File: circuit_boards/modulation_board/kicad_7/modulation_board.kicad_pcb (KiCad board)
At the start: 2 copper layers, 0 parts

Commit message: Progress on circuit boards
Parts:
- added C1001: 10u, Capacitor_THT:CP_Radial_D6.3mm_P2.50mm, B.Cu at (116.4, 143.8)
- added C1002: 10u, Capacitor_THT:CP_Radial_D6.3mm_P2.50mm, B.Cu at (95.3, 143.8)
- added C1003: 470n, Capacitor_SMD:C_0805_2012Metric, B.Cu at (86.1, 125.1)
- added C1004: 470n, Capacitor_SMD:C_0805_2012Metric, B.Cu at (89.9, 136.2)
- added C1005: 100n, Capacitor_SMD:C_0603_1608Metric, B.Cu at (90.9, 125.1)
- added C1006: 100n, Capacitor_SMD:C_0603_1608Metric, B.Cu at (84.9, 136.0)
- added C1007: 2u2, Capacitor_SMD:C_0805_2012Metric, B.Cu at (87.1, 106.3)
- added C1008: 100n, Capacitor_SMD:C_0603_1608Metric, B.Cu at (91.9, 106.3)
- added C1009: 100n, Capacitor_SMD:C_0603_1608Metric, B.Cu at (60.9, 109.2)
- added C1010: 100n, Capacitor_SMD:C_0603_1608Metric, B.Cu at (66.0, 109.2)
- added C1011: 100n, Capacitor_SMD:C_0603_1608Metric, B.Cu at (77.7, 141.0)
- added C1012: 100n, Capacitor_SMD:C_0603_1608Metric, B.Cu at (82.5, 141.0)
- added C1013: 100n, Capacitor_SMD:C_0603_1608Metric, B.Cu at (97.3, 51.4)
- added C1014: 100n, Capacitor_SMD:C_0603_1608Metric, B.Cu at (102.4, 51.4)
- added C1015: 100n, Capacitor_SMD:C_0603_1608Metric, B.Cu at (110.7, 79.7)
- added C1016: 100n, Capacitor_SMD:C_0603_1608Metric, B.Cu at (89.5, 73.8)
- added C1017: 100n, Capacitor_SMD:C_0603_1608Metric, B.Cu at (73.8, 164.9)
- added C1018: 100n, Capacitor_SMD:C_0603_1608Metric, B.Cu at (78.5, 176.8)
- added C301: 100n, Capacitor_SMD:C_0603_1608Metric, B.Cu at (121.4, 116.3)
- added C302: 4p3, Capacitor_SMD:C_0603_1608Metric, B.Cu at (125.2, 110.5)
- added C303: 4p3, Capacitor_SMD:C_0603_1608Metric, B.Cu at (125.2, 113.3)
- added C304: 100n, Capacitor_SMD:C_0603_1608Metric, B.Cu at (133.1, 78.2)
- added C305: 100n, Capacitor_SMD:C_0603_1608Metric, B.Cu at (148.8, 51.6)
- added C306: 100n, Capacitor_SMD:C_0603_1608Metric, B.Cu at (110.2, 115.8)
- added C307: 1u, Capacitor_SMD:C_0805_2012Metric, B.Cu at (106.9, 115.8)
- added C308: 10u, Capacitor_SMD:C_0805_2012Metric, B.Cu at (105.2, 112.3)
- added C309: 100n, Capacitor_SMD:C_0603_1608Metric, B.Cu at (121.4, 119.1)
- added C310: 10u, Capacitor_SMD:C_0805_2012Metric, B.Cu at (121.4, 122.2)
- added C401: 100n, Capacitor_SMD:C_0603_1608Metric, B.Cu at (57.7, 66.0)
- added C402: 100n, Capacitor_SMD:C_0603_1608Metric, B.Cu at (79.5, 65.8)
- added C403: 100n, Capacitor_SMD:C_0603_1608Metric, B.Cu at (101.6, 65.8)
- added C404: 100n, Capacitor_SMD:C_0603_1608Metric, B.Cu at (124.0, 65.5)
- added C405: 100n, Capacitor_SMD:C_0603_1608Metric, B.Cu at (57.1, 95.5)
- added C406: 100n, Capacitor_SMD:C_0603_1608Metric, B.Cu at (79.5, 94.7)
- added C407: 100n, Capacitor_SMD:C_0603_1608Metric, B.Cu at (101.6, 95.5)
- added C408: 100n, Capacitor_SMD:C_0603_1608Metric, B.Cu at (124.0, 96.0)
- added C409: 100n, Capacitor_SMD:C_0603_1608Metric, B.Cu at (109.2, 139.2)
- added C410: 100n, Capacitor_SMD:C_0603_1608Metric, B.Cu at (125.2, 138.7)
- added C411: 100n, Capacitor_SMD:C_0603_1608Metric, B.Cu at (142.7, 158.8)
- added C412: 100n, Capacitor_SMD:C_0603_1608Metric, B.Cu at (57.7, 36.8)
- added C413: 100n, Capacitor_SMD:C_0603_1608Metric, B.Cu at (84.8, 80.4)
- added C414: 100n, Capacitor_SMD:C_0603_1608Metric, B.Cu at (93.0, 77.6)
- added C501: 100n, Capacitor_SMD:C_0603_1608Metric, B.Cu at (111.0, 119.9)
- added C601: 10u, Capacitor_SMD:C_0805_2012Metric, B.Cu at (124.7, 91.4)
- added C602: 1u, Capacitor_SMD:C_0805_2012Metric, B.Cu at (109.0, 97.5)
- added C603: 10u, Capacitor_SMD:C_0805_2012Metric, B.Cu at (54.6, 84.6)
- added C604: 10u, Capacitor_SMD:C_0805_2012Metric, B.Cu at (54.6, 78.5)
- added C605: 1n, Capacitor_SMD:C_0603_1608Metric, B.Cu at (72.1, 110.5)
- added C606: 1n, Capacitor_SMD:C_0603_1608Metric, B.Cu at (54.7, 112.8)
- added C607: 1n, Capacitor_SMD:C_0603_1608Metric, B.Cu at (72.1, 102.1)
- added C608: 1n, Capacitor_SMD:C_0603_1608Metric, B.Cu at (54.7, 101.6)
- added C609: 100n, Capacitor_SMD:C_0603_1608Metric, B.Cu at (115.6, 87.5)
- added C610: 1u, Capacitor_SMD:C_0805_2012Metric, B.Cu at (115.6, 84.4)
- added C611: 100n, Capacitor_SMD:C_0603_1608Metric, B.Cu at (53.8, 119.9)
- added C612: 100n, Capacitor_SMD:C_0603_1608Metric, B.Cu at (109.0, 103.9)
- added C613: 100n, Capacitor_SMD:C_0603_1608Metric, B.Cu at (54.6, 74.4)
- added C614: 1u, Capacitor_SMD:C_0805_2012Metric, B.Cu at (109.0, 100.8)
- added C615: 100n, Capacitor_SMD:C_0603_1608Metric, B.Cu at (55.4, 137.9)
- added C616: 100n, Capacitor_SMD:C_0603_1608Metric, B.Cu at (54.1, 132.8)
- added C617: 100n, Capacitor_SMD:C_0603_1608Metric, B.Cu at (111.6, 174.0)
- added C618: 100n, Capacitor_SMD:C_0603_1608Metric, B.Cu at (146.8, 130.8)
- added C701: 100n, Capacitor_SMD:C_0603_1608Metric, B.Cu at (144.0, 104.7)
- added C801: 10n, Capacitor_SMD:C_0603_1608Metric, B.Cu at (77.7, 159.8)
- added C802: 47n COG, Capacitor_SMD:C_0805_2012Metric, B.Cu at (72.4, 176.5)
- added C803: 100p, Capacitor_SMD:C_0603_1608Metric, B.Cu at (87.9, 140.7)
- added C804: 100p, Capacitor_SMD:C_0603_1608Metric, B.Cu at (72.9, 143.5)
- added C805: 10u, Capacitor_SMD:C_0805_2012Metric, B.Cu at (48.1, 183.2)
- added C901: 100p, Capacitor_SMD:C_0603_1608Metric, B.Cu at (107.3, 43.4)
- added C902: 100p, Capacitor_SMD:C_0603_1608Metric, B.Cu at (93.0, 43.4)
- added C903: 100p, Capacitor_SMD:C_0603_1608Metric, B.Cu at (96.3, 65.9)
- added D301: 1N4148W, Diode_SMD:D_SOD-123, B.Cu at (141.2, 75.2)
- added D701: LED, LED_THT:LED_D3.0mm, F.Cu at (147.9, 40.0)
- added D702: LED, LED_THT:LED_D3.0mm, F.Cu at (147.9, 71.8)
- added D703: LED, LED_THT:LED_D3.0mm, F.Cu at (147.9, 100.3)
- added D704: LED, LED_THT:LED_D3.0mm, F.Cu at (85.1, 111.8)
- added D705: LED, LED_THT:LED_D3.0mm, F.Cu at (98.4, 134.0)
- added FB1001: 100R @ 100MHz, Inductor_SMD:L_0805_2012Metric, B.Cu at (90.9, 110.7)
- added FB1002: 100R @ 100MHz, Inductor_SMD:L_0805_2012Metric, B.Cu at (116.6, 120.7)
- added FB301: 1k@100MHz, Inductor_SMD:L_0805_2012Metric, B.Cu at (134.1, 66.0)
- added FB302: 1k@100MHz, Inductor_SMD:L_0805_2012Metric, B.Cu at (134.1, 63.0)
- added FB303: 1k@100MHz, Inductor_SMD:L_0805_2012Metric, B.Cu at (144.0, 43.2)
- added FB304: 1k@100MHz, Inductor_SMD:L_0805_2012Metric, B.Cu at (144.0, 51.3)
- added J1: MOD_BOARD_EXT_CON, custom_footprints:16_pin_IDC_header, B.Cu at (116.8, 45.1)
- added J2: VCO_BOARD_CON, custom_footprints:40_pin_IDC_header, B.Cu at (48.3, 48.9)
- added J3: VCF_BOARD_CON, custom_footprints:30_pin_IDC-Header, B.Cu at (64.1, 117.5)
- added J301: SWD_header, Connector_PinHeader_2.54mm:PinHeader_1x04_P2.54mm_Vertical, B.Cu at (107.7, 107.7)
- added J4: power_entry, custom_footprints:10_pin_IDC-Header, B.Cu at (101.6, 151.1)
- added Q801: MMBT3904, Package_TO_SOT_SMD:SOT-23, B.Cu at (57.8, 178.1)
- added R301: 220, Resistor_SMD:R_0603_1608Metric, B.Cu at (140.7, 71.6)
- added R302: 10k, Resistor_SMD:R_0603_1608Metric, B.Cu at (118.9, 107.4)
- added R303: 10k, Resistor_SMD:R_0603_1608Metric, B.Cu at (126.5, 73.2)
- added R304: 220, Resistor_SMD:R_0603_1608Metric, B.Cu at (95.8, 103.1)
- added R305: 22, Resistor_SMD:R_0603_1608Metric, B.Cu at (144.0, 46.0)
- added R306: 10, Resistor_SMD:R_0603_1608Metric, B.Cu at (144.0, 48.8)
- added R401: 5k6, Resistor_SMD:R_0603_1608Metric, B.Cu at (84.8, 77.6)
- added R402: 10k, Resistor_SMD:R_0603_1608Metric, B.Cu at (84.8, 83.2)
- added R501: 390, Resistor_SMD:R_0603_1608Metric, B.Cu at (139.9, 166.9)
- added R502: 100k, Resistor_SMD:R_0603_1608Metric, B.Cu at (117.3, 78.6)
- added R503: 100k, Resistor_SMD:R_0603_1608Metric, B.Cu at (103.8, 78.6)
- added R504: 100k, Resistor_SMD:R_0603_1608Metric, B.Cu at (117.3, 75.8)
- added R505: 10k, Resistor_SMD:R_0603_1608Metric, B.Cu at (103.8, 75.8)
- added R506: 1M, Resistor_SMD:R_0603_1608Metric, B.Cu at (117.3, 73.0)
- added R507: 1M, Resistor_SMD:R_0603_1608Metric, B.Cu at (103.8, 73.0)
- added R601: 2k7, Resistor_SMD:R_0603_1608Metric, B.Cu at (128.5, 87.4)
- added R602: 10k, Resistor_SMD:R_0603_1608Metric, B.Cu at (111.2, 87.5)
- added R603: 100k, Resistor_SMD:R_0603_1608Metric, B.Cu at (54.6, 81.5)
- added R604: 100k, Resistor_SMD:R_0603_1608Metric, B.Cu at (54.6, 87.6)
- added R605: 20k, Resistor_SMD:R_0603_1608Metric, B.Cu at (72.1, 107.7)
- added R606: 10k, Resistor_SMD:R_0603_1608Metric, B.Cu at (72.1, 113.3)
- added R607: 20k, Resistor_SMD:R_0603_1608Metric, B.Cu at (54.7, 110.0)
- added R608: 47k, Resistor_SMD:R_0603_1608Metric, B.Cu at (54.7, 107.2)
- added R609: 10k, Resistor_SMD:R_0603_1608Metric, B.Cu at (54.7, 115.6)
- added R610: 68k, Resistor_SMD:R_0603_1608Metric, B.Cu at (72.1, 104.9)
- added R611: 47k, Resistor_SMD:R_0603_1608Metric, B.Cu at (54.7, 104.4)
- added R701: 390, Resistor_SMD:R_0603_1608Metric, B.Cu at (149.1, 43.4)
- added R702: 390, Resistor_SMD:R_0603_1608Metric, B.Cu at (149.1, 74.9)
- added R703: 390, Resistor_SMD:R_0603_1608Metric, B.Cu at (149.1, 103.6)
- added R704: 390, Resistor_SMD:R_0603_1608Metric, B.Cu at (86.4, 115.1)
- added R705: 390, Resistor_SMD:R_0603_1608Metric, B.Cu at (99.6, 137.4)
- added R801: 20k, Resistor_SMD:R_0603_1608Metric, B.Cu at (57.7, 174.2)
- added R802: 20k, Resistor_SMD:R_0603_1608Metric, B.Cu at (52.8, 174.2)
- added R803: 100k, Resistor_SMD:R_0603_1608Metric, B.Cu at (86.4, 170.4)
- added R804: 27k, Resistor_SMD:R_0603_1608Metric, B.Cu at (86.4, 173.2)
- added R805: 150k, Resistor_SMD:R_0603_1608Metric, B.Cu at (82.0, 178.8)
- added R806: 100k, Resistor_SMD:R_0603_1608Metric, B.Cu at (86.4, 178.8)
- added R807: 100k, Resistor_SMD:R_0603_1608Metric, B.Cu at (82.0, 176.0)
- added R808: 100k, Resistor_SMD:R_0603_1608Metric, B.Cu at (82.0, 173.2)
- added R809: 10k, Resistor_SMD:R_0603_1608Metric, B.Cu at (65.3, 174.2)
- added R810: 270k, Resistor_SMD:R_0603_1608Metric, B.Cu at (86.4, 176.0)
- added R811: 47k, Resistor_SMD:R_0603_1608Metric, B.Cu at (65.3, 168.7)
- added R812: 270, Resistor_SMD:R_0603_1608Metric, B.Cu at (73.8, 162.1)
- added R813: 1M, Resistor_SMD:R_0603_1608Metric, B.Cu at (65.3, 171.4)
- added R814: 100k, Resistor_SMD:R_0603_1608Metric, B.Cu at (87.9, 149.1)
- added R815: 4k7, Resistor_SMD:R_0603_1608Metric, B.Cu at (73.7, 159.3)
- added R816: 100k, Resistor_SMD:R_0603_1608Metric, B.Cu at (111.6, 177.0)
- added R817: 200k, Resistor_SMD:R_0603_1608Metric, B.Cu at (87.9, 151.9)
- added R818: 100k, Resistor_SMD:R_0603_1608Metric, B.Cu at (87.9, 146.3)
- added R819: 200k, Resistor_SMD:R_0603_1608Metric, B.Cu at (87.9, 143.5)
- added R820: 3k9, Resistor_SMD:R_0603_1608Metric, B.Cu at (82.2, 164.9)
- added R821: 4k7, Resistor_SMD:R_0603_1608Metric, B.Cu at (86.5, 164.9)
- added R822: 10k, Resistor_SMD:R_0603_1608Metric, B.Cu at (78.1, 164.9)
- added R823: 12k, Resistor_SMD:R_0603_1608Metric, B.Cu at (82.2, 167.7)
- added R824: 4k7, Resistor_SMD:R_0603_1608Metric, B.Cu at (86.5, 167.7)
- added R825: 10k, Resistor_SMD:R_0603_1608Metric, B.Cu at (82.2, 162.1)
- added R826: 20k, Resistor_SMD:R_0603_1608Metric, B.Cu at (72.9, 149.1)
- added R827: 56k, Resistor_SMD:R_0603_1608Metric, B.Cu at (72.9, 146.3)
- added R828: 1k, Resistor_SMD:R_0603_1608Metric, B.Cu at (53.0, 179.8)
- added R901: 100k, Resistor_SMD:R_0603_1608Metric, B.Cu at (107.3, 49.0)
- added R902: 100k, Resistor_SMD:R_0603_1608Metric, B.Cu at (107.3, 51.8)
- added R903: 22k, Resistor_SMD:R_0603_1608Metric, B.Cu at (107.3, 54.6)
- added R904: 100k, Resistor_SMD:R_0603_1608Metric, B.Cu at (107.3, 46.2)
- added R905: 100k, Resistor_SMD:R_0603_1608Metric, B.Cu at (93.0, 49.0)
- added R906: 100k, Resistor_SMD:R_0603_1608Metric, B.Cu at (96.3, 71.5)
- added R907: 100k, Resistor_SMD:R_0603_1608Metric, B.Cu at (96.3, 74.3)
- added R908: 100k, Resistor_SMD:R_0603_1608Metric, B.Cu at (93.0, 46.2)
- added R909: 33k, Resistor_SMD:R_0603_1608Metric, B.Cu at (96.3, 68.7)
- added REF**: OSHW-Logo2_14.6x12mm_SilkScreen, Symbol:OSHW-Logo2_14.6x12mm_SilkScreen, B.Cu at (69.6, 62.5)
- added RV401: 100k, Potentiometer_THT:Potentiometer_Alpha_RD901F-40-00D_Single_Vertical, F.Cu at (55.9, 69.1)
- added RV402: 100k, Potentiometer_THT:Potentiometer_Alpha_RD901F-40-00D_Single_Vertical, F.Cu at (78.1, 69.1)
- added RV403: 100k, Potentiometer_THT:Potentiometer_Alpha_RD901F-40-00D_Single_Vertical, F.Cu at (100.4, 69.1)
- added RV404: 100k, Potentiometer_THT:Potentiometer_Alpha_RD901F-40-00D_Single_Vertical, F.Cu at (122.6, 69.1)
- added RV405: 100k, Potentiometer_THT:Potentiometer_Alpha_RD901F-40-00D_Single_Vertical, F.Cu at (55.9, 98.3)
- added RV406: 100k, Potentiometer_THT:Potentiometer_Alpha_RD901F-40-00D_Single_Vertical, F.Cu at (78.1, 98.3)
- added RV407: 100k, Potentiometer_THT:Potentiometer_Alpha_RD901F-40-00D_Single_Vertical, F.Cu at (100.4, 98.3)
- added RV408: 100k, Potentiometer_THT:Potentiometer_Alpha_RD901F-40-00D_Single_Vertical, F.Cu at (122.6, 98.3)
- added RV409: 100k, custom_footprints:Bourns_PTV09, F.Cu at (108.0, 141.5)
- added RV410: 100k, custom_footprints:Bourns_PTV09, F.Cu at (123.8, 141.5)
- added RV411: 100k, custom_footprints:Bourns_PTV09, F.Cu at (141.6, 161.8)
- added RV412: 100k, Potentiometer_THT:Potentiometer_Alpha_RD901F-40-00D_Single_Vertical, F.Cu at (55.9, 39.9)
- added RV601: 5k, Potentiometer_THT:Potentiometer_Bourns_3296W_Vertical, B.Cu at (77.4, 104.6)
- added RV602: 5k, Potentiometer_THT:Potentiometer_Bourns_3296W_Vertical, B.Cu at (64.5, 97.0)
- added RV603: 10k, Potentiometer_THT:Potentiometer_Alpha_RD901F-40-00D_Single_Vertical, F.Cu at (144.2, 133.2)
- added RV801: 10k, Potentiometer_THT:Potentiometer_Alpha_RD901F-40-00D_Single_Vertical, F.Cu at (62.3, 177.7)
- added RV802: 10k, Potentiometer_THT:Potentiometer_Alpha_RD901F-40-00D_Single_Vertical, F.Cu at (87.7, 161.8)
- added RV803: 5k, Potentiometer_THT:Potentiometer_Bourns_3296W_Vertical, B.Cu at (97.3, 166.9)
- added RV804: 5k, Potentiometer_THT:Potentiometer_Bourns_3296W_Vertical, B.Cu at (54.9, 163.8)
- added RV805: 5k, Potentiometer_THT:Potentiometer_Bourns_3296W_Vertical, B.Cu at (102.9, 168.1)
- added RV901: 100k, Potentiometer_THT:Potentiometer_Alpha_RD901F-40-00D_Single_Vertical, F.Cu at (78.1, 39.9)
- added RV902: 100k, Potentiometer_THT:Potentiometer_Alpha_RD901F-40-00D_Single_Vertical, F.Cu at (100.4, 39.9)
- added RV903: 100k, Potentiometer_THT:Potentiometer_Alpha_RD901F-40-00D_Single_Vertical, F.Cu at (122.6, 39.9)
- added SW501: E-Switch_EG2301B, custom_footprints:E-Switch_EG2301, F.Cu at (141.0, 32.4)
- added SW502: E-Switch_EG2301B, custom_footprints:E-Switch_EG2301, F.Cu at (141.0, 61.6)
- added SW503: E-Switch_EG2301B, custom_footprints:E-Switch_EG2301, F.Cu at (141.0, 90.8)
- added SW504: E-Switch_EG2301B, custom_footprints:E-Switch_EG2301, F.Cu at (54.0, 125.7)
- added SW505: E-Switch_EG2301B, custom_footprints:E-Switch_EG2301, F.Cu at (77.5, 125.7)
- added SW506: E-Switch_EG2301B, custom_footprints:E-Switch_EG2301, F.Cu at (99.7, 122.6)
- added SW507: E-Switch_EG2301B, custom_footprints:E-Switch_EG2301, F.Cu at (132.1, 117.5)
- added SW508: 5511M12, custom_footprints:E_Switch_5511M12, F.Cu at (144.1, 174.0)
- added SW801: E-Switch_EG2301B, custom_footprints:E-Switch_EG2301, F.Cu at (93.3, 178.4)
- added SW802: SR1712F-0204, custom_footprints:SR1712F_rotary_switch, F.Cu at (115.6, 170.2)
- added TP1001: V+, TestPoint:TestPoint_Keystone_5000-5004_Miniature, B.Cu at (120.7, 152.4)
- added TP1002: V-, TestPoint:TestPoint_Keystone_5000-5004_Miniature, B.Cu at (80.8, 150.9)
- added TP1003: GND, TestPoint:TestPoint_Bridge_Pitch7.62mm_Drill1.3mm, B.Cu at (144.8, 142.2)
- added TP1004: +5v, TestPoint:TestPoint_Keystone_5000-5004_Miniature, B.Cu at (65.0, 183.1)
- added TP1005: -5v, TestPoint:TestPoint_Keystone_5000-5004_Miniature, B.Cu at (71.4, 183.1)
- added TP1006: 3v3, TestPoint:TestPoint_Keystone_5000-5004_Miniature, B.Cu at (125.5, 147.8)
- added TP601: DAC_Vref, TestPoint:TestPoint_Keystone_5000-5004_Miniature, B.Cu at (126.7, 78.7)
- added TP602: PITCH_CV, TestPoint:TestPoint_Keystone_5000-5004_Miniature, B.Cu at (81.8, 107.2)
- added TP603: S&H_CV, TestPoint:TestPoint_Keystone_5000-5004_Miniature, B.Cu at (70.5, 87.0)
- added TP801: MODOSC_Vref, TestPoint:TestPoint_Keystone_5000-5004_Miniature, B.Cu at (55.4, 183.1)
- added TP802: MODOSC, TestPoint:TestPoint_Keystone_5000-5004_Miniature, B.Cu at (53.1, 150.4)
- added U1: STM32L412K8Ux, Package_DFN_QFN:QFN-32-1EP_5x5mm_P0.5mm_EP3.45x3.45mm, B.Cu at (114.8, 113.0)
- added U10: TL072, Package_SO:SOIC-8_3.9x4.9mm_P1.27mm, B.Cu at (63.4, 104.4)
- added U1001: L78L05_SOT89, Package_TO_SOT_SMD:SOT-89-3, B.Cu at (88.4, 119.6)
- added U1002: L79L05_SOT89, Package_TO_SOT_SMD:SOT-89-3, B.Cu at (88.4, 131.0)
- added U1003: L78L33_SOT89, Package_TO_SOT_SMD:SOT-89-3, B.Cu at (89.7, 101.3)
- added U11: 74HC595, Package_SO:SOIC-16_3.9x9.9mm_P1.27mm, B.Cu at (144.0, 112.1)
- added U12: SSI2130, Package_DFN_QFN:QFN-32-1EP_4x4mm_P0.4mm_EP2.9x2.9mm, B.Cu at (75.9, 171.0)
- added U13: TL072, Package_SO:SOIC-8_3.9x4.9mm_P1.27mm, B.Cu at (80.0, 146.1)
- added U14: TL072, Package_SO:SOIC-8_3.9x4.9mm_P1.27mm, B.Cu at (99.8, 46.5)
- added U15: MCP6002-xSN, Package_SO:SOIC-8_3.9x4.9mm_P1.27mm, B.Cu at (89.5, 69.0)
- added U2: VO0600T, Package_SO:SOIC-8_3.9x4.9mm_P1.27mm, B.Cu at (133.1, 73.4)
- added U3: SN74LV1T34DBV, Package_TO_SOT_SMD:SOT-23-5, B.Cu at (148.8, 47.8)
- added U5: 74HC4067PW, Package_SO:TSSOP-24_4.4x7.8mm_P0.65mm, B.Cu at (93.0, 84.2)
- added U6: 74HC4067PW, Package_SO:TSSOP-24_4.4x7.8mm_P0.65mm, B.Cu at (111.3, 127.2)
- added U601: LM4040C-2.5, Package_TO_SOT_SMD:SOT-23, B.Cu at (124.7, 87.1)
- added U7: MCP6002-xSN, Package_SO:SOIC-8_3.9x4.9mm_P1.27mm, B.Cu at (110.7, 74.9)
- added U8: DAC8162xDGSx, Package_SO:VSSOP-10_3x3mm_P0.5mm, B.Cu at (115.3, 102.6)
- added U801: LM4040C-2.5, Package_TO_SOT_SMD:SOT-23, B.Cu at (48.1, 178.9)
- added U9: MCP48CVB28T-E/ML, Package_DFN_QFN:QFN-20-1EP_4x4mm_P0.5mm_EP2.7x2.7mm, B.Cu at (114.6, 92.4)
- added Y301: 32_768KHZ, Crystal:Crystal_SMD_MicroCrystal_CC7V-T1A-2Pin_3.2x1.5mm, B.Cu at (121.4, 112.0)
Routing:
- net +3.3V: track 0.00 -> 432.8 mm, vias 0 -> 16
- net +3.3VA: track 0.00 -> 329.0 mm, vias 0 -> 3
- net +5V: track 0.00 -> 312.4 mm, vias 0 -> 8
- net +12V: track 0.00 -> 231.3 mm, vias 0 -> 4
- net -12V: track 0.00 -> 197.9 mm, vias 0 -> 5
- net /S_AND_H: track 0.00 -> 196.6 mm, vias 0 -> 1
- net -5V: track 0.00 -> 193.8 mm, vias 0 -> 6
- net /PITCH_CV: track 0.00 -> 189.4 mm, vias 0 -> 3
- net /EXT_MODOSC_CV_IN: track 0.00 -> 177.5 mm, vias 0 -> 1
- net /S_AND_H_MIXER: track 0.00 -> 176.5 mm, vias 0 -> 2
- net /digital_ctl_generators/discrete_controls/S_AND_H_TRIG_SRC_A: track 0.00 -> 143.2 mm, vias 0 -> 1
- net /digital_ctl_generators/discrete_controls/S_AND_H_TRIG_SRC_B: track 0.00 -> 140.4 mm, vias 0 -> 2
- net /WHITE_NOISE: track 0.00 -> 137.3 mm, vias 0 -> 1
- net /VCF_ENV: track 0.00 -> 134.7 mm, vias 0 -> 2
- net /MOD_OSC: track 0.00 -> 133.8 mm
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- added copper zone on B.Cu, net GND
- added copper zone on F.Cu, net GND
- added copper zone on In2.Cu, net GND
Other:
- board outline added: 111.8 x 165.1 mm
- copper layers 2 -> 4
- board text added: "+3V3"
- board text added: "+5V"
- board text added: "-5V"
- board text added: "1"
- board text added: "DAC VREF"
- board text added: "DC POWER INPUT"
- board text added: "GATE IN"
- board text added: "GND"
- board text added: "MICRO-OX Modulation Board rev 0 2023-03-21"
- board text added: "MIDI 1V/OCT"
- board text added: "MIDI IN P4"
- board text added: "MIDI IN P5"
- board text added: "MIDI THRU P4"
- board text added: "MIDI THRU P5"
- board text added: "MODOSC"
- board text added: "MODOSC BASE"
- board text added: "MODOSC CV"
- board text added: "MODOSC H.F."
- board text added: "MODOSC SCALE"
- board text added: "MODOSC VREF"
- board text added: "Open source documentation: github.com/JordanAceto/micro_ox"
- board text added: "S&H 1V/OCT"
- board text added: "SWD"
- board text added: "V+"
- board text added: "V-"

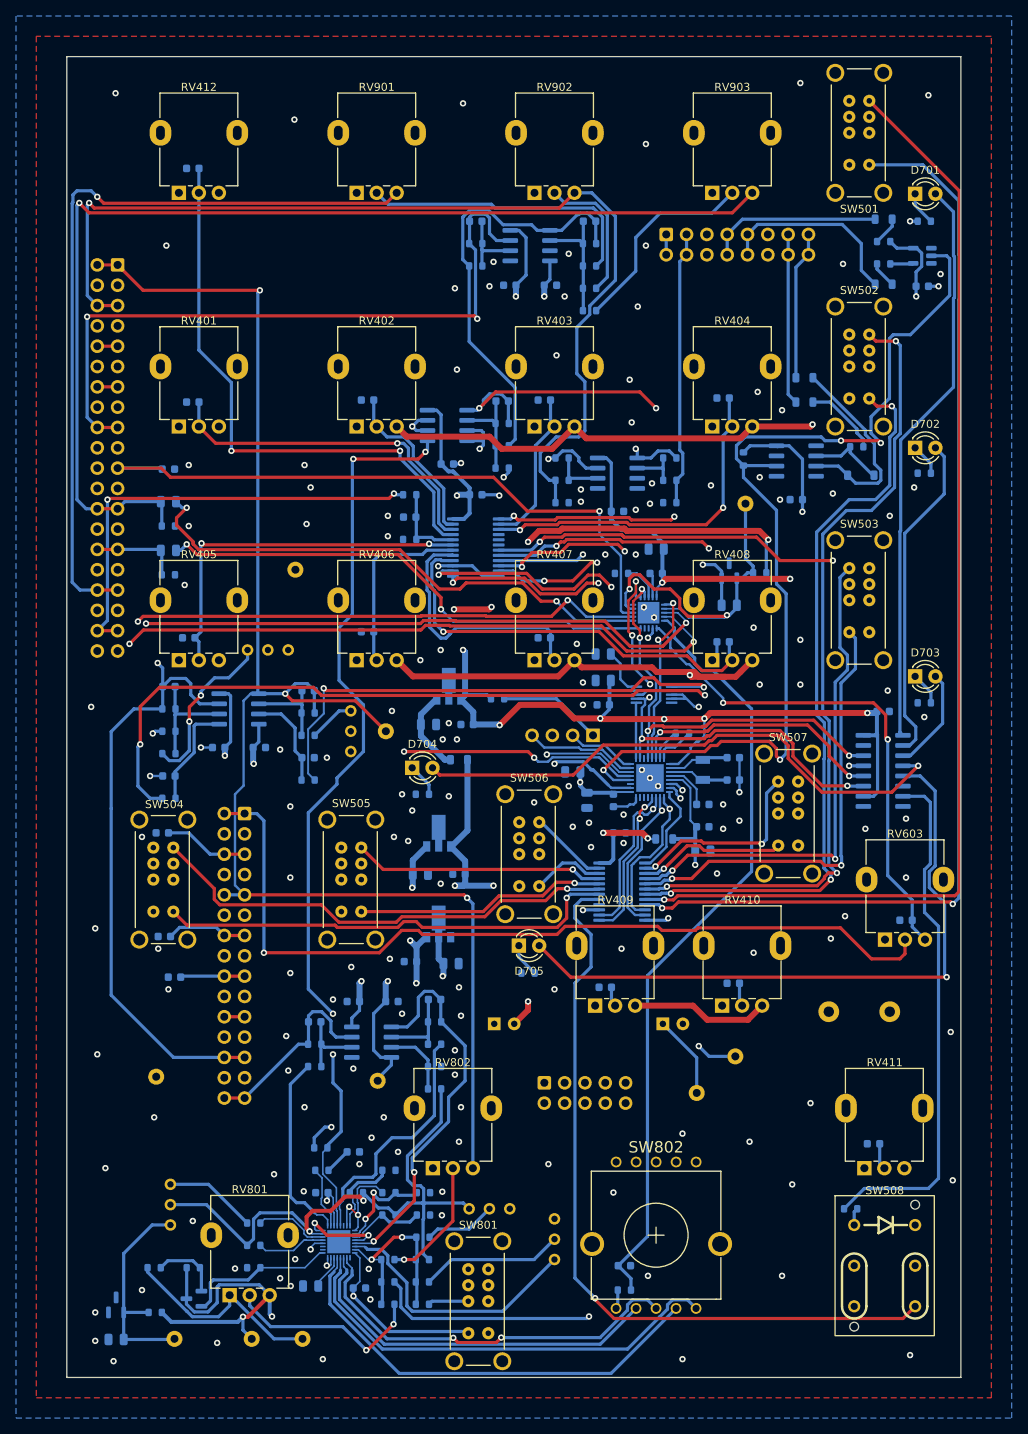
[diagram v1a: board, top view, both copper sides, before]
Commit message: Tweaks to mod board, add debug pin
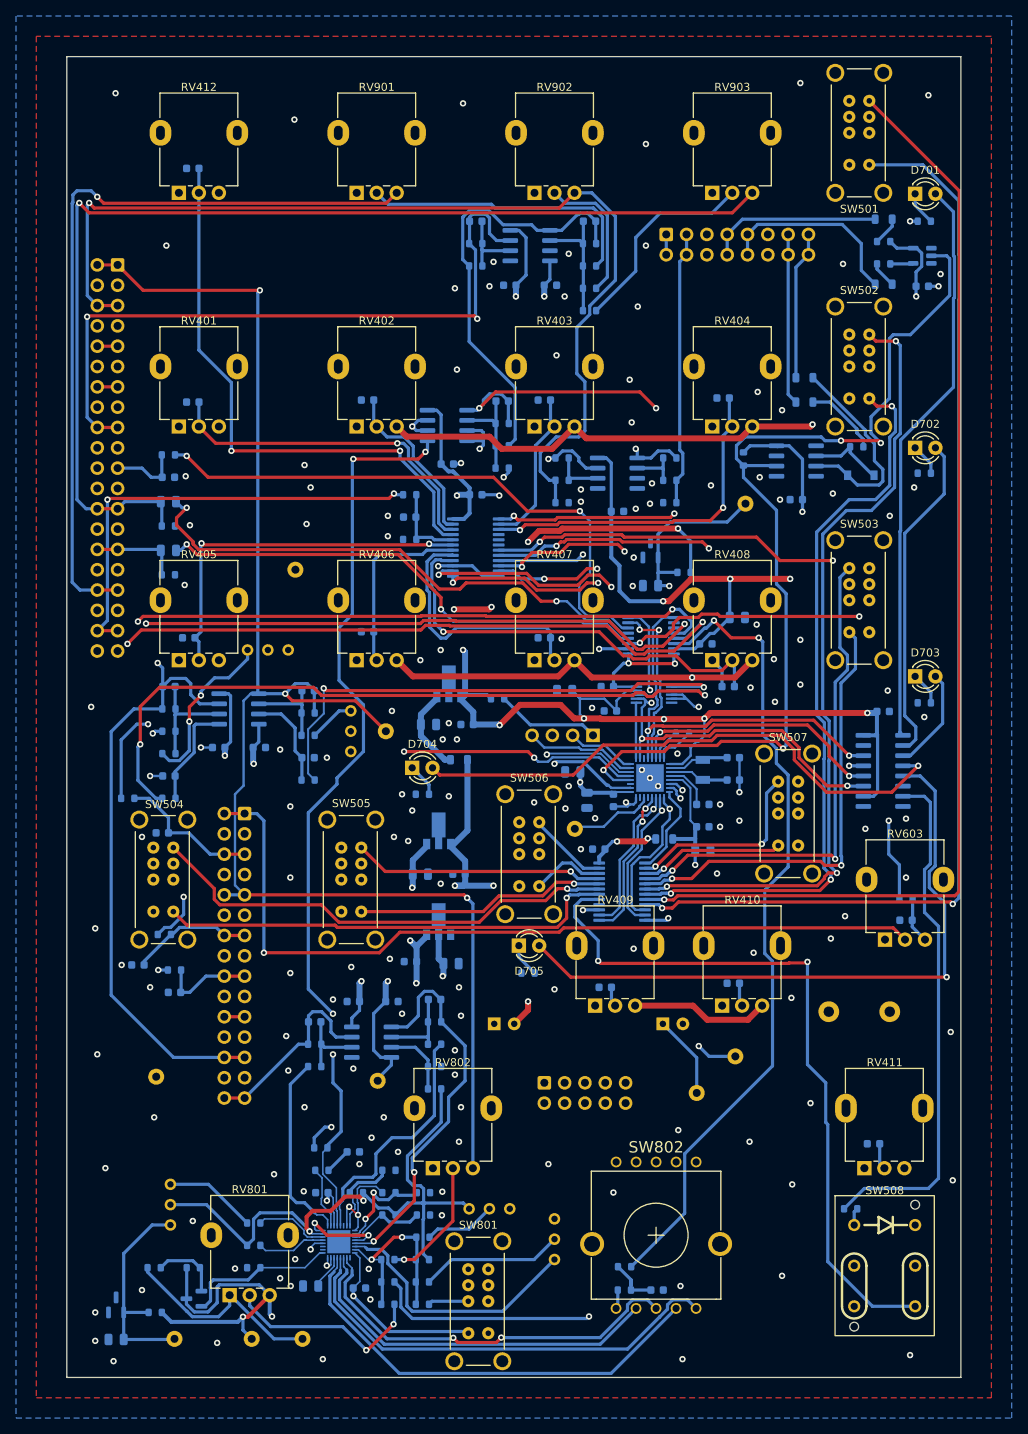
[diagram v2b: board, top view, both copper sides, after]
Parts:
- removed U601: LM4040C-2.5, Package_TO_SOT_SMD:SOT-23
- added R603: 1k, Resistor_SMD:R_0603_1608Metric, B.Cu at (54.1, 132.6)
- added R604: 1k, Resistor_SMD:R_0603_1608Metric, B.Cu at (55.4, 137.0)
- added R605: 1k, Resistor_SMD:R_0603_1608Metric, B.Cu at (111.6, 174.1)
- added R606: 1k, Resistor_SMD:R_0603_1608Metric, B.Cu at (54.6, 72.6)
- added R607: 1k, Resistor_SMD:R_0603_1608Metric, B.Cu at (146.8, 128.0)
- added TP301: debug_pin, TestPoint:TestPoint_Keystone_5000-5004_Miniature, B.Cu at (105.4, 119.4)
- added U4: LM4040C-2.5, Package_TO_SOT_SMD:SOT-23, B.Cu at (114.9, 84.5)
- C601: value 10u -> 1u
- C602: value 1u -> 100n; footprint Capacitor_SMD:C_0805_2012Metric -> Capacitor_SMD:C_0603_1608Metric
- C610: value 1u -> 10u
- C611, C615, C617: value 100n -> 10n
- R601: value 2k7 -> 1k
- R602: value 10k -> 1k
- RV603, RV801, RV802: value 10k -> 100k
- U9: value MCP48CVB28T-E/ML -> DAC128S085CIMT; footprint Package_DFN_QFN:QFN-20-1EP_4x4mm_P0.5mm_EP2.7x2.7mm -> Package_SO:TSSOP-16_4.4x5mm_P0.65mm
- moved C617 113.8 mm to (54.6, 75.4)
- moved C616 75.8 mm to (115.7, 177.0), turned to 0 degrees
- moved R602 67.8 mm to (49.5, 115.6), turned to 0 degrees
- moved C613 62.1 mm to (50.8, 136.4), turned to 180 degrees
- moved C609 10.8 mm to (121.8, 96.3), turned to 0 degrees
- moved R601 9.46 mm to (119.1, 87.3)
- moved C408 5.62 mm to (124.6, 101.6)
- moved C614 4.99 mm to (104.1, 102.1)
- moved C610 4.62 mm to (114.9, 89.0)
- moved C602 4.10 mm to (109.5, 101.6)
- moved C501 3.29 mm to (108.4, 121.9), turned to 180 degrees
- moved U9 2.89 mm to (114.9, 95.2)
- moved C615 1.91 mm to (55.4, 139.8)
- moved C601 1.83 mm to (125.7, 93.0), turned to 0 degrees
- moved C612 1.17 mm to (109.9, 104.6)
- renumbered R604 to R608, R603 to R609, R605 to R610, R606 to R611, R610 to R612, R608 to R613, R607 to R614, R609 to R615, R611 to R616
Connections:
- net /digital_ctl_generators/analog_controls/POT_MUX.COM_0 renamed /digital_ctl_generators/analog_controls/POT_MUX.COM_ANALOG
- net /digital_ctl_generators/analog_controls/POT_MUX.COM_1 renamed /digital_ctl_generators/analog_controls/POT_MUX.COM_DISCRETE
- C601 pad 1: Net-(U601-K) -> +3.3V
- C602 pad 1: Net-(U8-VREFH/VREFOUT) -> Net-(U4-K)
- C603 pad 1: Net-(U9-VOUT_7) -> Net-(C603-Pad1)
- C604 pad 1: Net-(U9-VOUT_5) -> Net-(C604-Pad1)
- C610 pad 1: +3.3V -> Net-(U4-K)
- C613 pad 1: /MOD_ENV -> /FEEDBACK_CV
- C616 pad 1: /FEEDBACK_CV -> /digital_ctl_generators/MIDI_MOD_WHEEL
- C617 pad 1: /digital_ctl_generators/MIDI_MOD_WHEEL -> /MOD_ENV
- C618 pad 1: Net-(U9-VOUT_6) -> Net-(C618-Pad1)
- R601 pad 2: Net-(U601-K) -> Net-(U4-K)
- R602 pad 1: Net-(U9-~{LAT_0}/HVC) -> Net-(U9-VOUT_A)
- R602 pad 2: GND -> /VCA_ENV
- RV603 pad 3: Net-(U9-VOUT_6) -> Net-(C618-Pad1)
- TP601 pad 1: Net-(U601-K) -> Net-(U4-K)
- U1 pad 14: unconnected-(U1-PB0-Pad14) -> Net-(U1-PB0)
- U8 pad 10: Net-(U8-VREFH/VREFOUT) -> Net-(U4-K)
- U9 pad 1: /digital_ctl_generators/DAC/DAC_SPI.~{CS_1} -> /digital_ctl_generators/DAC/DAC_SPI.SDO
- U9 pad 10: Net-(U9-VOUT_7) -> GND
- U9 pad 11: Net-(U9-VOUT_5) -> Net-(U9-VOUT_H)
- U9 pad 12: /FEEDBACK_CV -> Net-(C603-Pad1)
- U9 pad 13: /MOD_ENV -> Net-(C604-Pad1)
- U9 pad 14: Net-(U601-K) -> Net-(U9-VOUT_E)
- U9 pad 15: unconnected-(U9-SDO-Pad15) -> /digital_ctl_generators/DAC/DAC_SPI.~{CS_1}
- U9 pad 2: Net-(U601-K) -> unconnected-(U9-DOUT-Pad2)
- U9 pad 3: /VCA_ENV -> Net-(U9-VOUT_A)
- U9 pad 4: /VCF_ENV -> Net-(U9-VOUT_B)
- U9 pad 5: /digital_ctl_generators/MIDI_MOD_WHEEL -> Net-(U9-VOUT_C)
- U9 pad 6: Net-(U9-VOUT_6) -> Net-(U9-VOUT_D)
- U9 pad 7: GND -> +3.3V
- U9 pad 8: unconnected-(U9-NC-Pad8) -> Net-(U4-K)
- U9 pad 9: unconnected-(U9-NC-Pad9) -> Net-(U4-K)
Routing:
- net Net-(U9-VOUT_C): track 0.00 -> 125.4 mm, vias 0 -> 3
- net /VCF_ENV: track 134.7 -> 11.6 mm, vias 2 -> 0
- net Net-(U9-VOUT_B): track 0.00 -> 117.4 mm, vias 0 -> 3
- net /FEEDBACK_CV: track 118.2 -> 15.3 mm, vias 2 -> 0
- net Net-(U9-VOUT_D): track 0.00 -> 101.8 mm, vias 0 -> 2
- net /VCA_ENV: track 117.1 -> 17.8 mm, vias 2 -> 0
- net Net-(U9-VOUT_A): track 0.00 -> 96.5 mm, vias 0 -> 3
- net /digital_ctl_generators/MIDI_MOD_WHEEL: track 96.8 -> 6.59 mm
- net /MOD_ENV: track 85.8 -> 11.4 mm, vias 1 -> 0
- net Net-(U9-VOUT_E): track 0.00 -> 73.9 mm, vias 0 -> 2
- net Net-(U9-VOUT_H): track 0.00 -> 68.2 mm, vias 0 -> 3
- net Net-(C604-Pad1): track 0.00 -> 67.2 mm, vias 0 -> 2
- net Net-(U9-VOUT_5): track 67.2 -> 0.00 mm, vias 2 -> 0
- net Net-(U9-VOUT_6): track 64.2 -> 0.00 mm, vias 2 -> 0
- net Net-(U9-VOUT_7): track 63.6 -> 0.00 mm, vias 2 -> 0
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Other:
- board text added: "MICRO-OX Modulation Board rev 0 2023-04-16"
- board text removed: "MICRO-OX Modulation Board rev 0 2023-03-21"
